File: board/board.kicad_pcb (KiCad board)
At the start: 2 copper layers, 21 x 13 mm, 1 part

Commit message: initial
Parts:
- added C11: 1uF, Capacitor_SMD:C_0603_1608Metric, F.Cu at (150.9, 106.3)
- added C12: 1uF, Capacitor_SMD:C_0603_1608Metric, F.Cu at (150.9, 107.8)
- added C13: 1uF, Capacitor_SMD:C_0603_1608Metric, F.Cu at (168.3, 105.6)
- added C14: 1uF, Capacitor_SMD:C_0603_1608Metric, F.Cu at (168.3, 107.2)
- added C15: 1uF, Capacitor_SMD:C_0603_1608Metric, F.Cu at (168.3, 108.7)
- added C16: 1uF, Capacitor_SMD:C_0603_1608Metric, F.Cu at (168.3, 110.2)
- added C17: 1uF, Capacitor_SMD:C_0603_1608Metric, F.Cu at (168.3, 111.8)
- added C18: 0.1uF, Capacitor_SMD:C_0603_1608Metric, F.Cu at (151.0, 112.1)
- added C19: 0.1uF, Capacitor_SMD:C_0603_1608Metric, F.Cu at (147.8, 110.6)
- added C20: 0.1uF, Capacitor_SMD:C_0603_1608Metric, F.Cu at (147.8, 112.1)
- added C21: 0.1uF, Capacitor_SMD:C_0603_1608Metric, F.Cu at (158.9, 95.8)
- added C22: 0.1uF, Capacitor_SMD:C_0603_1608Metric, F.Cu at (155.9, 95.8)
- added C23: 1uF, Capacitor_SMD:C_0603_1608Metric, F.Cu at (174.6, 111.7)
- added C24: 10uF, Capacitor_SMD:C_0603_1608Metric, F.Cu at (177.5, 103.3)
- added C25: 10uF, Capacitor_SMD:C_0603_1608Metric, F.Cu at (175.9, 103.3)
- added C26: 100nF, Capacitor_SMD:C_0603_1608Metric, F.Cu at (174.4, 103.3)
- added D1: MMSZ5248B, Diode_SMD:D_SOD-123, F.Cu at (148.9, 101.7)
- added D10: C3 LED, LED_SMD:LED_0603_1608Metric, F.Cu at (177.6, 107.2)
- added D11: C2 LED, LED_SMD:LED_0603_1608Metric, F.Cu at (177.6, 108.7)
- added D12: C1 LED, LED_SMD:LED_0603_1608Metric, F.Cu at (177.6, 110.2)
- added D2: BAS316, Diode_SMD:D_SOD-323, F.Cu at (147.9, 106.3)
- added D3: SMBJ26A-13-F, Diode_SMD:D_SMB, F.Cu at (181.9, 108.6)
- added D9: C4 LED, LED_SMD:LED_0603_1608Metric, F.Cu at (177.6, 105.6)
- added J1: 022_battery_cells, on_edge:on_edge_2x05_device, F.Cu at (140.0, 96.5)
- added J2: 022_battery_cells, on_edge:on_edge_2x05_host, F.Cu at (185.0, 96.5)
- added Q2: CSD18534Q5A, Package_TO_SOT_SMD:TDSON-8-1, F.Cu at (161.0, 99.4)
- added Q3: CSD18534Q5A, Package_TO_SOT_SMD:TDSON-8-1, F.Cu at (153.8, 99.4)
- added R10: 33R, Resistor_SMD:R_0603_1608Metric, F.Cu at (171.4, 105.6)
- added R15: 33R, Resistor_SMD:R_0603_1608Metric, F.Cu at (171.4, 107.2)
- added R16: 33R, Resistor_SMD:R_0603_1608Metric, F.Cu at (171.4, 108.7)
- added R17: 33R, Resistor_SMD:R_0603_1608Metric, F.Cu at (171.4, 110.2)
- added R18: 33R, Resistor_SMD:R_0603_1608Metric, F.Cu at (171.4, 111.7)
- added R19: 1k, Resistor_SMD:R_0603_1608Metric, F.Cu at (150.9, 104.8)
- added R20: 15mΩ SHUNT RLP25FEER015, Resistor_SMD:R_Shunt_Vishay_WSK2512_6332Metric_T1.19mm, F.Cu at (169.2, 101.9)
- added R21: 100R, Resistor_SMD:R_0603_1608Metric, F.Cu at (172.0, 99.2)
- added R22: 100R, Resistor_SMD:R_0603_1608Metric, F.Cu at (151.0, 110.6)
- added R23: 5.1k, Resistor_SMD:R_0603_1608Metric, F.Cu at (167.7, 97.3)
- added R24: 5.1k, Resistor_SMD:R_0603_1608Metric, F.Cu at (147.8, 108.1)
- added R25: 10M, Resistor_SMD:R_0603_1608Metric, F.Cu at (165.4, 98.0)
- added R26: 3M, Resistor_SMD:R_0603_1608Metric, F.Cu at (147.0, 100.8)
- added R27: 1M, Resistor_SMD:R_0603_1608Metric, F.Cu at (147.0, 103.9)
- added R28: 470k, Resistor_SMD:R_0603_1608Metric, F.Cu at (163.7, 111.6)
- added R29: 100k, Resistor_SMD:R_0603_1608Metric, F.Cu at (163.7, 108.7)
- added R30: 10k, Resistor_SMD:R_0603_1608Metric, F.Cu at (163.7, 105.7)
- added R31: 10k, Resistor_SMD:R_0603_1608Metric, F.Cu at (163.7, 107.2)
- added R32: 10k, Resistor_SMD:R_0603_1608Metric, F.Cu at (163.7, 110.2)
- added R66: 1k, Resistor_SMD:R_0603_1608Metric, F.Cu at (174.6, 105.6)
- added R67: 1k, Resistor_SMD:R_0603_1608Metric, F.Cu at (174.6, 107.2)
- added R68: 1k, Resistor_SMD:R_0603_1608Metric, F.Cu at (174.6, 108.7)
- added R69: 1k, Resistor_SMD:R_0603_1608Metric, F.Cu at (174.6, 110.2)
- added TH1: 103AT 10k, Connector_PinHeader_2.54mm:PinHeader_1x02_P2.54mm_Vertical, F.Cu at (156.0, 115.0)
- added U3: BQ7791501PWR, Package_SO:TSSOP-24_4.4x7.8mm_P0.65mm, F.Cu at (157.0, 108.7)
- moved LOGO1 17.2 mm to (143.9, 115.0)
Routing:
- net /balancer/C0: track 0.00 -> 134.7 mm, vias 0 -> 8
- net GND: track 0.00 -> 98.0 mm, vias 0 -> 2
- net /balancer/C4: track 0.00 -> 87.3 mm, vias 0 -> 3
- net /balancer/C2: track 0.00 -> 64.4 mm, vias 0 -> 3
- net /balancer/C1: track 0.00 -> 64.2 mm, vias 0 -> 3
- net /balancer/C3: track 0.00 -> 64.0 mm, vias 0 -> 3
- net /balancer/VC4: track 0.00 -> 39.2 mm
- net /balancer/VC3: track 0.00 -> 34.1 mm
- net /balancer/VC2: track 0.00 -> 32.5 mm
- net /balancer/VC1: track 0.00 -> 31.8 mm
- net /balancer/BMS_SRN: track 0.00 -> 29.8 mm, vias 0 -> 2
- net Net-(R20-Pad3): track 0.00 -> 21.7 mm
- net /balancer/VC0: track 0.00 -> 21.4 mm
- net Net-(C21-Pad1): track 0.00 -> 21.1 mm
- net Net-(U3-CHG): track 0.00 -> 21.0 mm, vias 0 -> 2
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- added copper zone on F.Cu, net GND
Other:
- board size 21 x 13 mm -> 45 x 29 mm

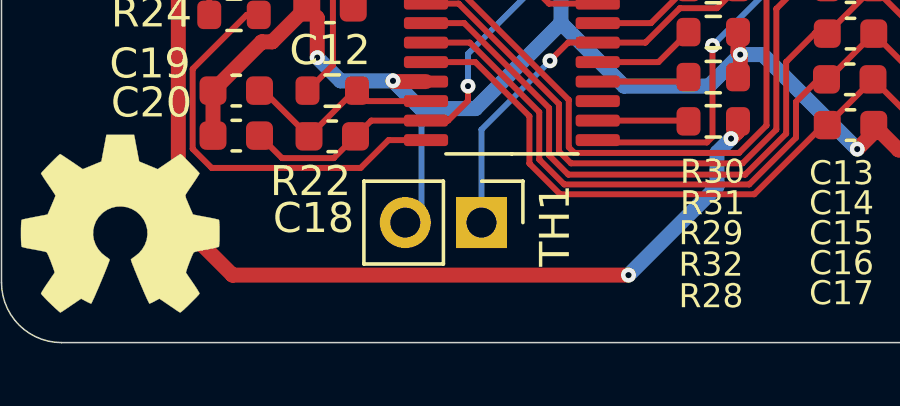
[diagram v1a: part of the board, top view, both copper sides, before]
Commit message: added board number on silk screen
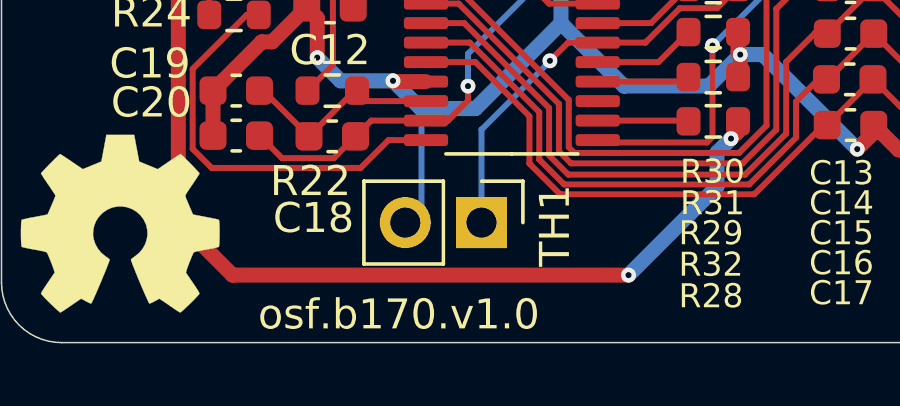
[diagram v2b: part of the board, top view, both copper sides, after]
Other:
- board text added: "osf.b170.v1.0"
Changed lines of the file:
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@@
 		(layer "Edge.Cuts")
+	)
+	(gr_text "osf.b170.v1.0"
+		(at 148.55 118.65 0)
+		(layer "F.SilkS")
+		(effects
+			(font
+				(size 1 1)
+				(thickness 0.15)
+			)
+			(justify left bottom)
+		)
 	)
 	(segment
